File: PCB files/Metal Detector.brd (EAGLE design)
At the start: 85.1 x 100.3 mm, 110 parts, among them IC1 NE5534AD, IC2 BQ24133RGYR, IC3 TPS54228DDAR, IC4 ESP32-WROOM-32UE-N4, IC7 TLV1117-33IDCYR, J2 DG128-7.5, Q1 IRF740, Q11 MMBT3904, Q2 IRF740, Q3 IRF9630, Q4 IRF740, Q9 MMBT3904, X2 DC21MMX

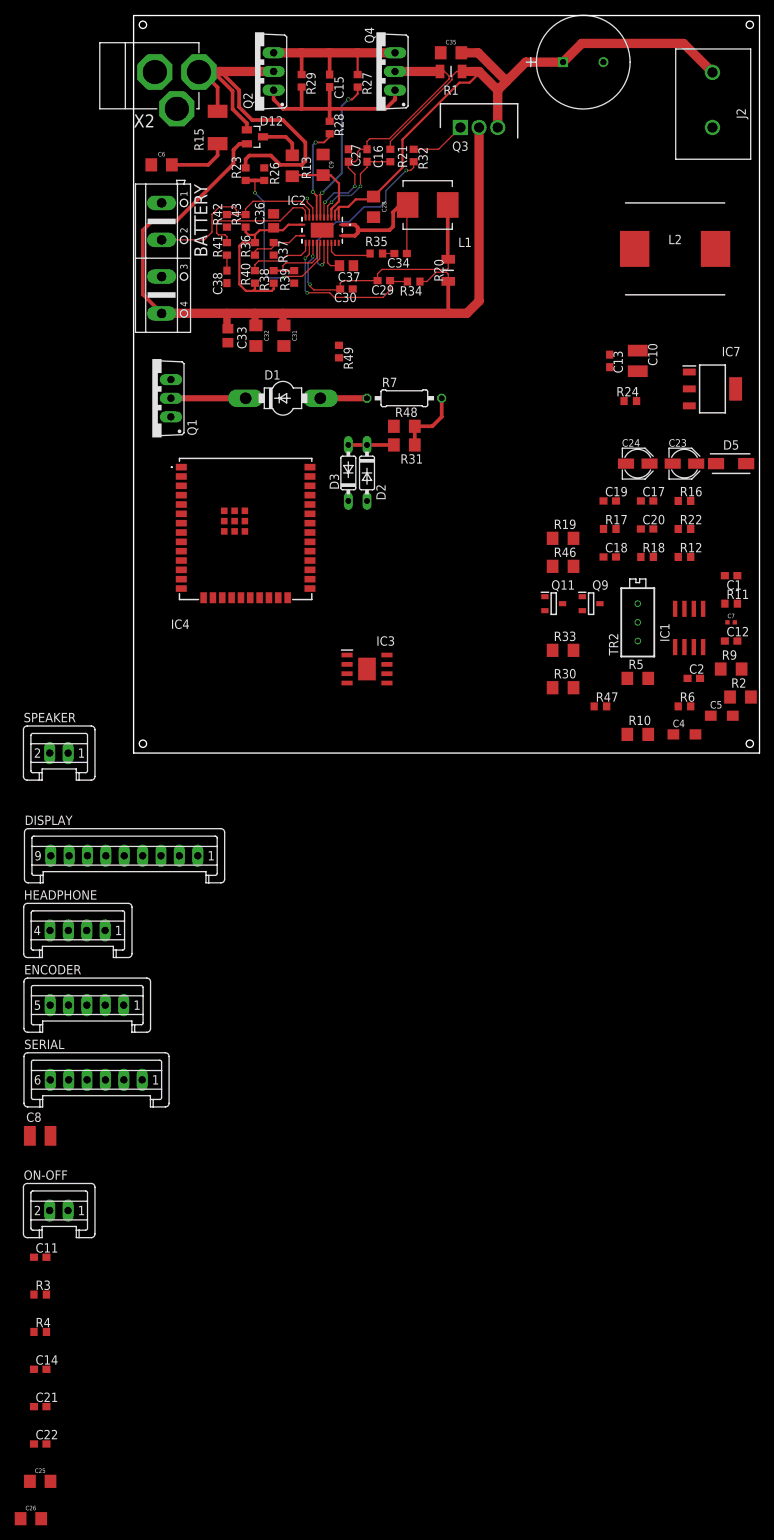
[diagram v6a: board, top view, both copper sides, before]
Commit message: Add files via upload
Designed 5V, 3.3V power circuit and signal processing circuit after that repositioned component I will do microprossesor connection and repositioning on next section
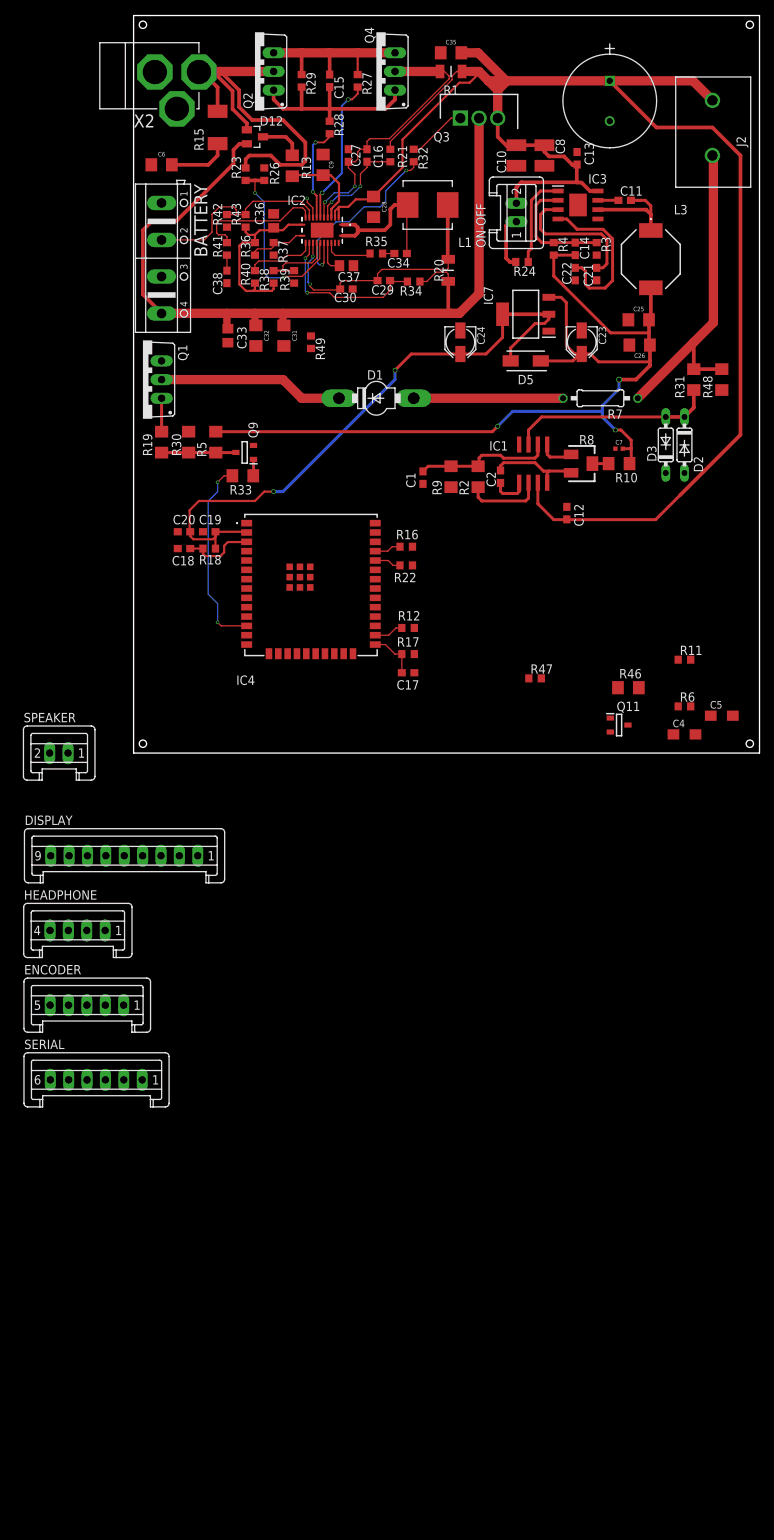
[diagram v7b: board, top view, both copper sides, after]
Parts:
- removed L2: SRP1265A-4R7M, SRP1265A-4R7M:INDM135125X640N
- removed TR2: 100K, rcl:RTRIM3296X
- added L3: SRU8043-4R7Y, SRU8043-330Y:SRU8043330Y
- added R8: 3224W-1-104E, 3224W-1-104E:3224W-1-105E
- moved C26 179.8 mm to (68.8, 55.5), turned to 180 degrees
- moved C25 177.7 mm to (68.7, 58.9), turned to 180 degrees
- moved C22 175.0 mm to (60.1, 65.2), turned to 270 degrees
- moved C21 171.6 mm to (63.0, 65.2), turned to 270 degrees
- moved C14 168.9 mm to (60.1, 68.6), turned to 270 degrees
- moved C11 164.3 mm to (66.8, 75.2)
- moved R4 163.0 mm to (57.1, 68.6), turned to 270 degrees
- moved R3 161.1 mm to (63.0, 68.6), turned to 90 degrees
- moved C8 150.0 mm to (55.9, 81.3), turned to 270 degrees
- moved ON-OFF 149.3 mm to (52.1, 73.5), turned to 270 degrees
- moved IC3 69.3 mm to (60.5, 74.5)
- moved R5 65.8 mm to (11.2, 42.3), turned to 270 degrees
- moved C20 63.0 mm to (6.86, 30.1)
- moved R30 60.9 mm to (7.49, 42.3), turned to 270 degrees
- moved R18 59.6 mm to (10.3, 27.8)
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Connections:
- net N$10: now also R8.2; no longer TR2.2
- net N$11: now also R8.3; no longer TR2.3
- net N$19: now also L3.1; no longer L2.1
- net N$9: now also R8.1; no longer TR2.1
- net VCC: now also L3.2; no longer L2.2
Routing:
- net VCC: track 124.1 -> 384.9 mm, vias 0 -> 3
- net VCCIO: track 0.00 -> 86.3 mm, vias 0 -> 2
- net N$7: track 9.26 -> 44.8 mm
- net IO27: track 0.00 -> 26.6 mm, vias 0 -> 2
- net N$33: track 0.00 -> 22.3 mm
- net N$1: track 6.20 -> 28.1 mm
- net N$30: track 0.00 -> 19.2 mm
- net N$12: track 0.00 -> 18.9 mm
- net N$24: track 0.00 -> 16.2 mm
- net N$6: track 10.2 -> 25.2 mm
- net IO4: track 0.00 -> 14.7 mm
- net N$19: track 0.00 -> 14.2 mm
- net N$4: track 6.35 -> 20.3 mm
- net N$17: track 0.00 -> 12.7 mm
- net N$11: track 0.00 -> 12.7 mm
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
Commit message: Add files via upload
All schematic and board design process is done after that upload BOM file, 3rd view docs and manufacturing files
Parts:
- removed C7: 10uF, SparkFun-Capacitors:0402-TIGHT
- added C39: 10uF, rcl:C0603
- R2: value 1mΩ -> 0.01Ω
- R30, R31: value 10KΩ -> 10kΩ
- moved SERIAL 96.0 mm to (35.1, 42.8), turned to 180 degrees
- moved C5 67.0 mm to (14.2, 17.9), turned to 180 degrees
- moved C4 63.2 mm to (14.2, 20.2), turned to 180 degrees
- moved R6 58.1 mm to (19.3, 23.2)
- moved DISPLAY 52.9 mm to (47.0, 7.62)
- moved ENCODER 51.1 mm to (22.9, 7.62)
- moved HEADPHONE 43.9 mm to (8.89, 16.5), turned to 90 degrees
- moved C1 37.8 mm to (67.9, 12.7), turned to 0 degrees
- moved R47 36.6 mm to (19.3, 19.9)
- moved SPEAKER 35.9 mm to (8.89, 30.5), turned to 90 degrees
- moved R9 32.4 mm to (67.8, 16.5), turned to 180 degrees
- moved R11 29.1 mm to (45.8, 13.7), turned to 180 degrees
- moved R2 27.2 mm to (67.8, 20.2), turned to 0 degrees
- moved R46 26.9 mm to (58.4, 34.3), turned to 90 degrees
- moved C2 22.9 mm to (67.8, 23.2), turned to 180 degrees
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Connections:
- net GND: now also C39.2; no longer C7.1
- net VCC: now also C39.1; no longer C7.2
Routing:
- net GND: track 0.00 -> 112.1 mm, vias 0 -> 15
- net VCC: track 384.9 -> 462.9 mm
- net IO35: track 2.92 -> 70.0 mm, vias 1 -> 4
- net VCCIO: track 86.3 -> 132.2 mm, vias 2 -> 3
- net IO0: track 6.69 -> 46.2 mm
- net IO4: track 14.7 -> 50.2 mm, vias 0 -> 2
- net SENSOR_VP: track 0.00 -> 31.7 mm, vias 0 -> 1
- net IO23: track 0.00 -> 30.7 mm, vias 0 -> 1
- net SENSOR_VN: track 0.00 -> 28.9 mm, vias 0 -> 1
- net IO22: track 0.00 -> 28.7 mm, vias 0 -> 1
- net EN: track 9.81 -> 37.4 mm, vias 0 -> 2
- net IO34: track 0.00 -> 26.2 mm, vias 0 -> 1
- net IO33: track 0.00 -> 24.8 mm
- net IO18: track 0.00 -> 23.3 mm, vias 0 -> 1
- net IO5: track 0.00 -> 20.8 mm, vias 0 -> 1
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- added copper zone on layer 1, net GND
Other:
- board size 85.1 x 100.3 mm -> 85.1 x 96.5 mm
